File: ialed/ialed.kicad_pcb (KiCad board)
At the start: 2 copper layers, 20 x 24 mm, 9 parts, among them Q1 2N7002

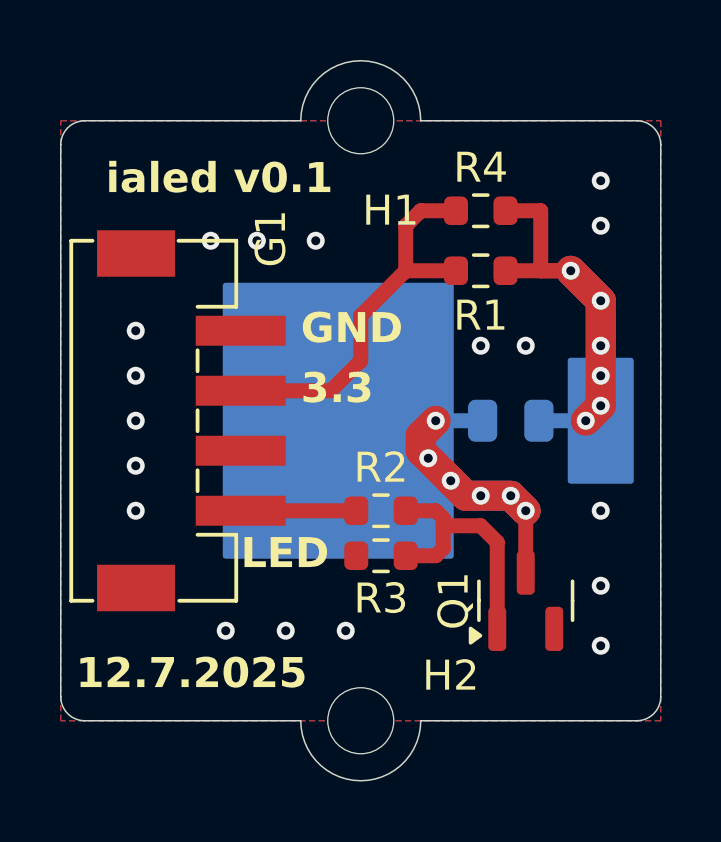
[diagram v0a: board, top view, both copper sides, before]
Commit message: ialed v0.2: new version 0.2 including production data
I added a second small read LED to the free seed connector pin.
The production started on 16.9.2025 with a panel process a jlcpcb.
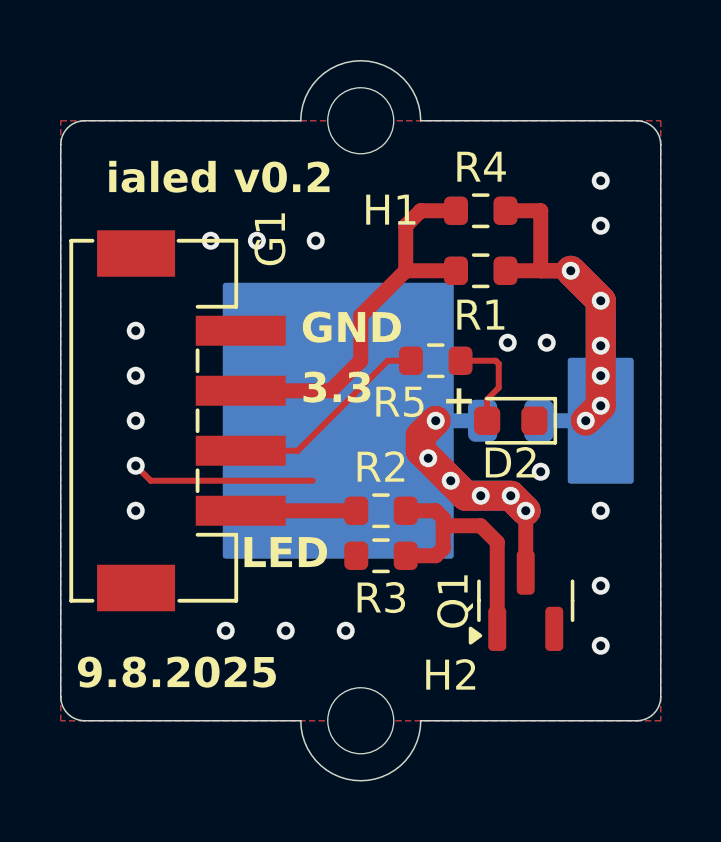
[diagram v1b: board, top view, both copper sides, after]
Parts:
- added D2: KT-0603R, Diode_SMD:D_0603_1608Metric, F.Cu at (15.0, 10.0)
- added R5: 470R, Resistor_SMD:R_0603_1608Metric, F.Cu at (12.5, 8.00)
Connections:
- G1 pad 2: unconnected-(G1-Pad2) -> Net-(G1-Pad2)
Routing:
- net Net-(G1-Pad2): track 0.00 -> 6.92 mm
- net GND: track 0.00 -> 6.11 mm, vias 18 -> 19
- net Net-(D2-A): track 0.00 -> 3.38 mm
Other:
- board text added: "+"
- board text added: "9.8.2025"
- board text added: "ialed v0.2"
- board text removed: "12.7.2025"
- board text removed: "ialed v0.1"
